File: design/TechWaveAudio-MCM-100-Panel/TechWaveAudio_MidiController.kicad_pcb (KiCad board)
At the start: 2 copper layers, 60.6 x 128.5 mm, 0 parts

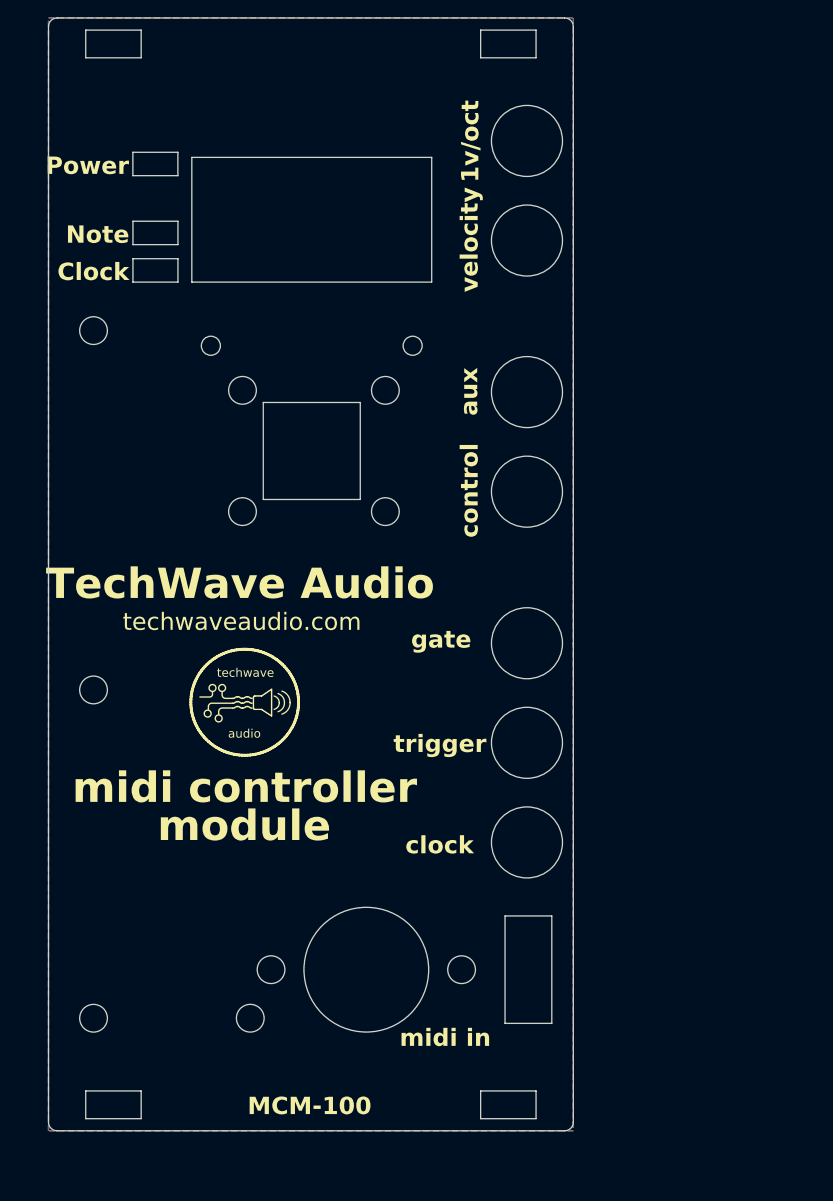
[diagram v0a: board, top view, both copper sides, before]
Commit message: updates for v 2.0.0 (#3)
* use quad DAC / rotary encoder

* cleanups and refactoring

* updaed new menu system w/ ext

* add ex outputs to hw controller

* run testing / calbibration on startup

* working hardware; outputs

* cleanups and refactoring

* hardware design updates for 2.0.0

* set extension sense

* update expansion;  ensure ex state is properly set

* better 7554 ; spi; i2c control; test all outputs selection

* update dashboard display for extension output

* better responsiveness; fix crashes; midi command queue

* fix ex sense; fix clock led menu

* cleanups and code documentation

* addtional cleanups and code documentation

* fix note on/vel 0 as note off event

* fix build startup; fix dashboard; fix display show/hide

* cleanups; remove specific note/vel/out hardware output

* fix sense expansion on reset

* code docs and cleanups; fix release build

* add display brightness control

* screen brightness; clean routs; xtra clock divs

* update boot screen; add show boot / about to testing

* docs update for 2.0
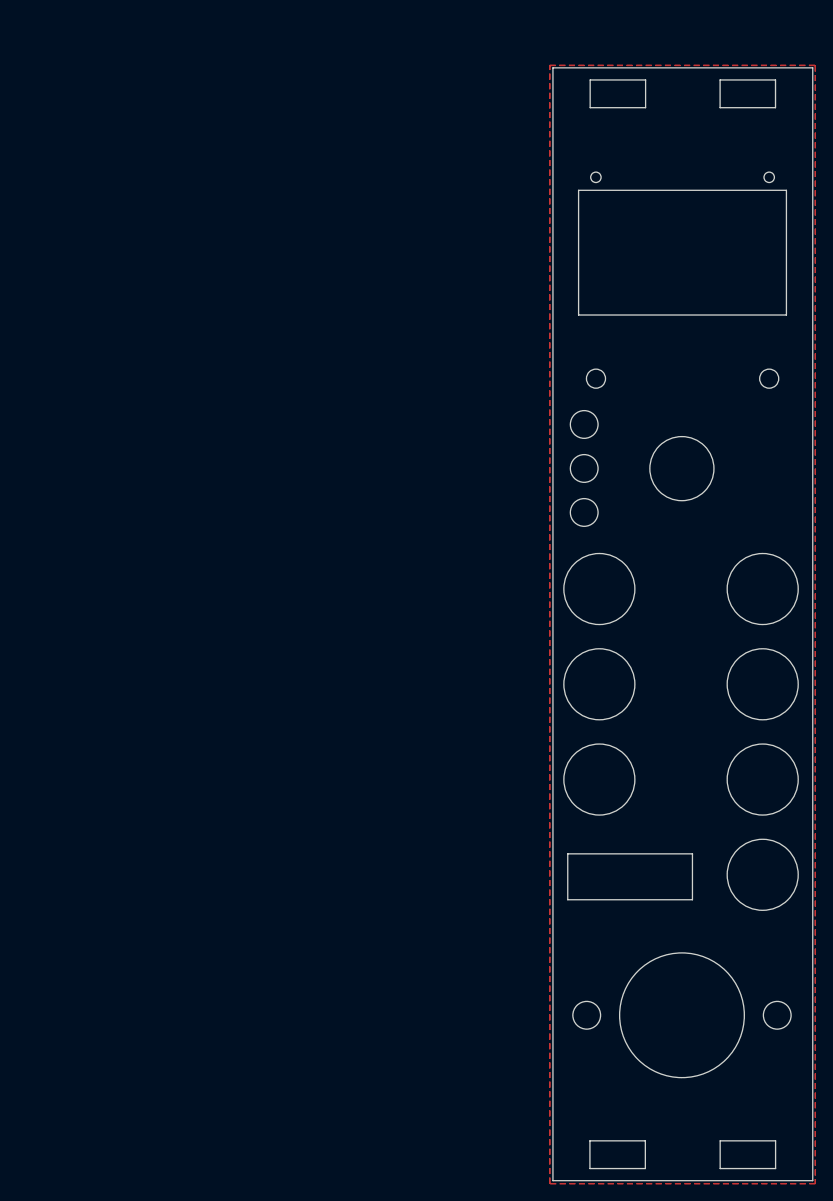
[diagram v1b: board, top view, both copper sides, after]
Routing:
- removed copper zone on B.Cu, net (none)
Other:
- board size 60.6 x 128.5 mm -> 30 x 128.5 mm
- board text added: "MIDI to CV Module"
- board text added: "Out 1"
- board text added: "Out 2"
- board text removed: "Audio Jack"
- board text removed: "Clock"
- board text removed: "Note"
- board text removed: "Power"
- board text removed: "audio"
- board text removed: "aux"
- board text removed: "control"
- board text removed: "midi controller"
- board text removed: "module"
- board text removed: "techwave"
